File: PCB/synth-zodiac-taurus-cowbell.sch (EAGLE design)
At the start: 67 parts, among them Q1 NPN, Q2 NPN, U1 TL071, U3 ATmega328P-AU, X1 16MHz, X2 16MHz, X3 16MHz

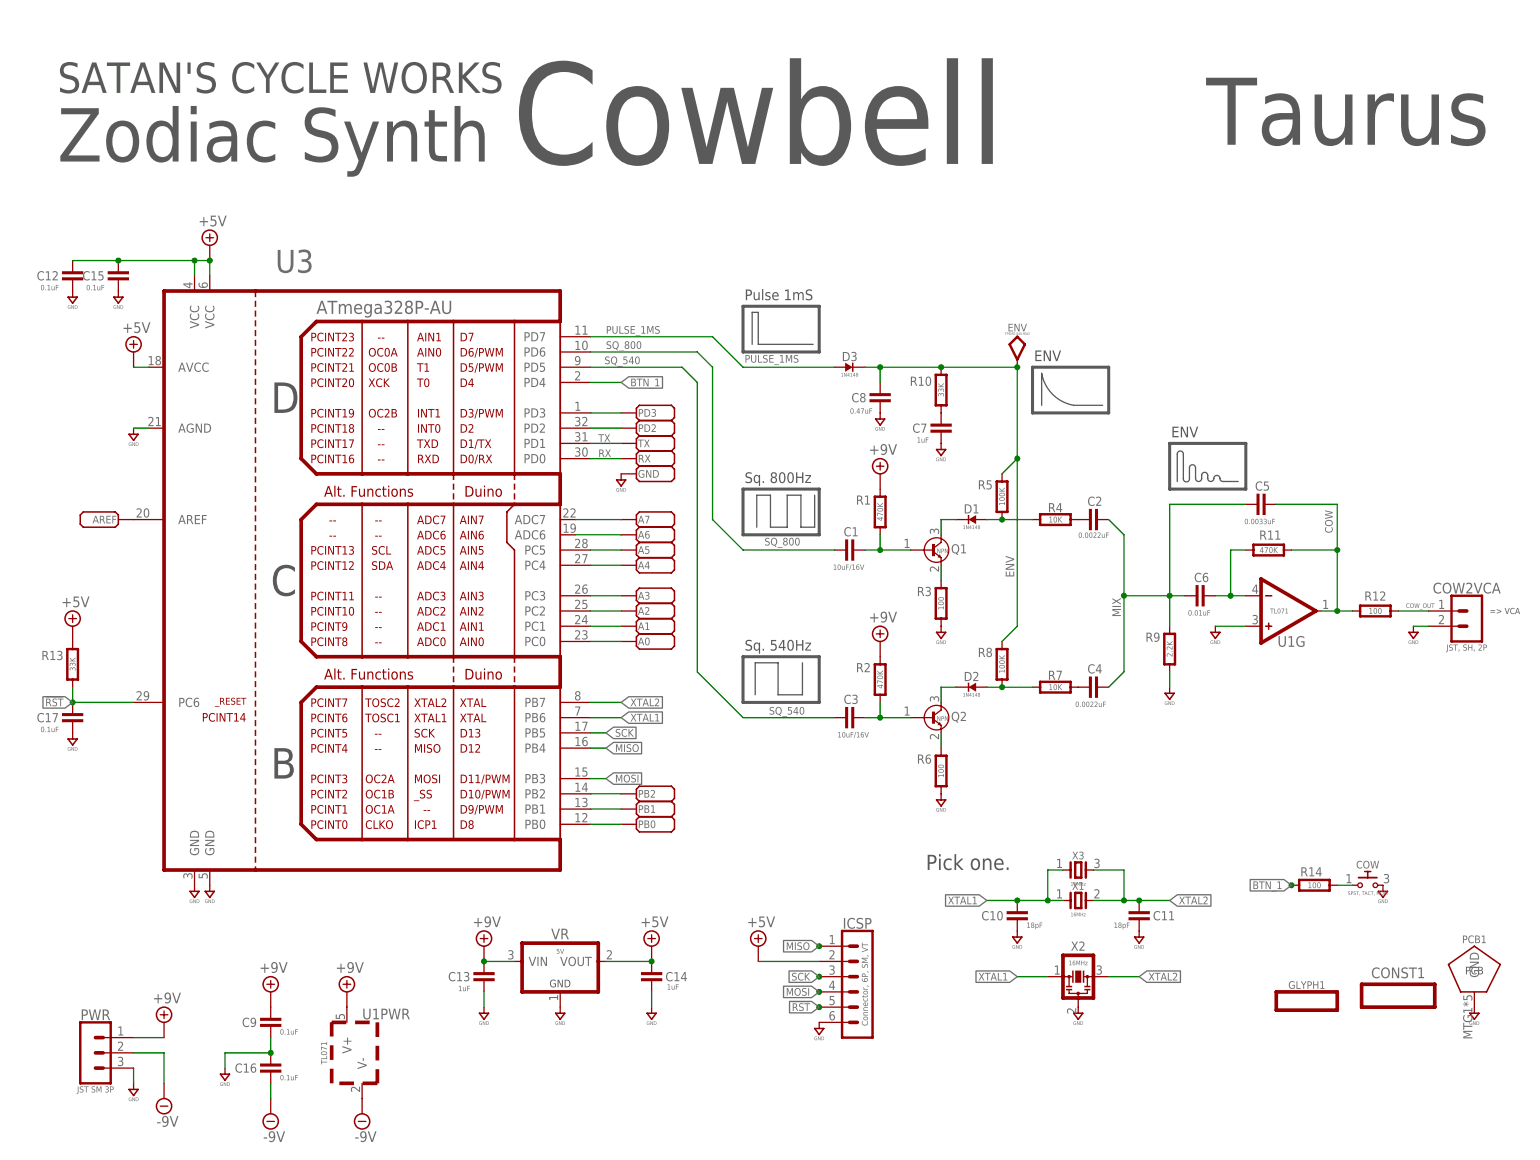
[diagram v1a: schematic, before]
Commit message: Tune values and some schematic visual tweaks.
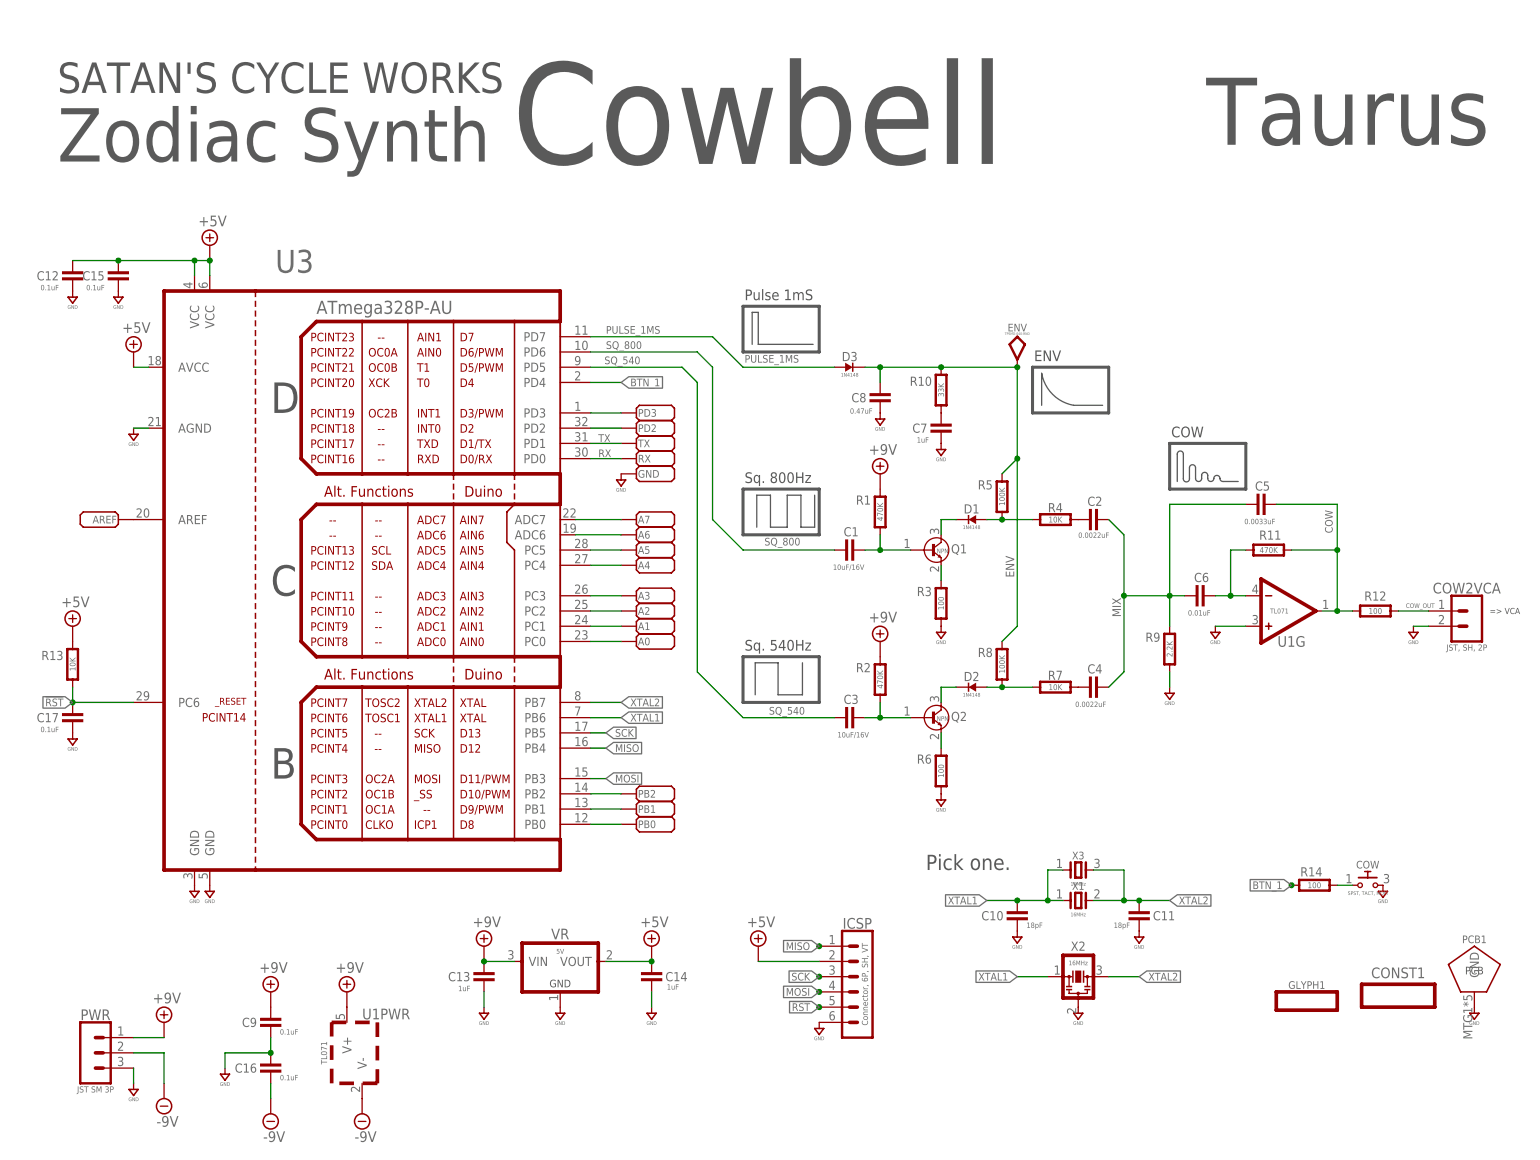
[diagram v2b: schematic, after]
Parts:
- ICSP: value Connector, 6P, SM, VT -> Connector, 6P, SH, VT
- R13: value 33K -> 10K
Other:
- note added: "COW"
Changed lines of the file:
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@@
 <part name="SUPPLY21" library="supply" library_urn="urn:adsk.eagle:library:10485988" deviceset="GND" device=""/>
 <part name="SUPPLY22" library="supply" library_urn="urn:adsk.eagle:library:10485988" deviceset="GND" device=""/>
-<part name="R13" library="rlc" library_urn="urn:adsk.eagle:library:4192893" deviceset="RESISTOR" device="0603" package3d_urn="urn:adsk.eagle:package:4193040/5" value="33K"/>
+<part name="R13" library="rlc" library_urn="urn:adsk.eagle:library:4192893" deviceset="RESISTOR" device="0603" package3d_urn="urn:adsk.eagle:package:4193040/5" value="10K"/>
 <part name="SUPPLY23" library="supply" library_urn="urn:adsk.eagle:library:10485988" deviceset="+5V" device=""/>
 <part name="C12" library="rlc" library_urn="urn:adsk.eagle:library:4192893" deviceset="CAPACITOR" device="0603" package3d_urn="urn:adsk.eagle:package:4193021/5" value="0.1uF"/>
@@
 <part name="SUPPLY39" library="supply" library_urn="urn:adsk.eagle:library:10485988" deviceset="GND" device=""/>
 <part name="GLYPH1" library="circuit-monkey-zodiac" library_urn="urn:adsk.eagle:library:36060312" deviceset="GLYPH" device="-TAURUS" package3d_urn="urn:adsk.eagle:package:41522816/2"/>
-<part name="ICSP" library="con-jst" library_urn="urn:adsk.eagle:library:7191852" deviceset="06P" device="-SM-VT-SMT" package3d_urn="urn:adsk.eagle:package:41517274/3" value="Connector, 6P, SM, VT"/>
+<part name="ICSP" library="con-jst" library_urn="urn:adsk.eagle:library:7191852" deviceset="06P" device="-SM-VT-SMT" package3d_urn="urn:adsk.eagle:package:41517274/3" value="Connector, 6P, SH, VT"/>
 <part name="SUPPLY40" library="supply" library_urn="urn:adsk.eagle:library:10485988" deviceset="GND" device=""/>
 <part name="SUPPLY41" library="supply" library_urn="urn:adsk.eagle:library:10485988" deviceset="+5V" device=""/>
@@
 <wire x1="198.882" y1="110.998" x2="199.39" y2="110.49" width="0.127" layer="97" curve="90"/>
 <wire x1="199.39" y1="110.49" x2="201.93" y2="110.49" width="0.127" layer="97"/>
-<text x="190.754" y="117.856" size="1.778" layer="97">ENV</text>
+<text x="190.754" y="117.856" size="1.778" layer="97">COW</text>
 <text x="121.92" y="180.34" size="16.9164" layer="97" ratio="15" align="top-center">Cowbell</text>
 <text x="5.08" y="172.72" size="8.89" layer="97" ratio="15" align="top-left">Zodiac Synth</text>
